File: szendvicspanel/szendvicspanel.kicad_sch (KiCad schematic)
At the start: 2 parts

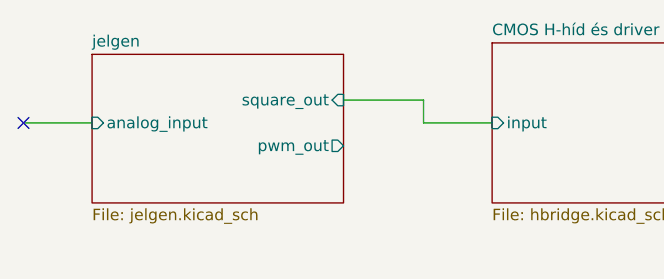
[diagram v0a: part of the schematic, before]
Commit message: Projekt átnevezése
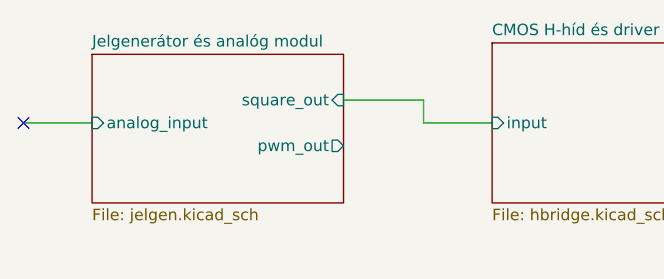
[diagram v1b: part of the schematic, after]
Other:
- sheet jelgen renamed Jelgenerátor és analóg modul
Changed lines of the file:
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@@
 			(color 0 0 0 0.0000)
 		)
-		(property "Sheetname" "jelgen"
+		(property "Sheetname" "Jelgenerátor és analóg modul"
 			(at 54.61 37.3884 0)
 			(effects
@@
 		)
 		(instances
-			(project "lebegteto_analog"
+			(project "szendvicspanel"
 				(path "/69584044-3e78-46a7-9ace-309a005e8329"
 					(page "2")
@@
 		)
 		(instances
-			(project "lebegteto_analog"
+			(project "szendvicspanel"
 				(path "/69584044-3e78-46a7-9ace-309a005e8329"
 					(page "4")

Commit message: Footprintek
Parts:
- LS1, LS2: footprint (none) -> Connector_PinHeader_1.27mm:PinHeader_1x02_P1.27mm_Horizontal
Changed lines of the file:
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@@
 			)
 		)
-		(property "Footprint" ""
+		(property "Footprint" "Connector_PinHeader_1.27mm:PinHeader_1x02_P1.27mm_Horizontal"
 			(at 181.991 55.88 0)
 			(effects
@@
 			)
 		)
-		(property "Footprint" ""
+		(property "Footprint" "Connector_PinHeader_1.27mm:PinHeader_1x02_P1.27mm_Horizontal"
 			(at 181.991 40.64 0)
 			(effects

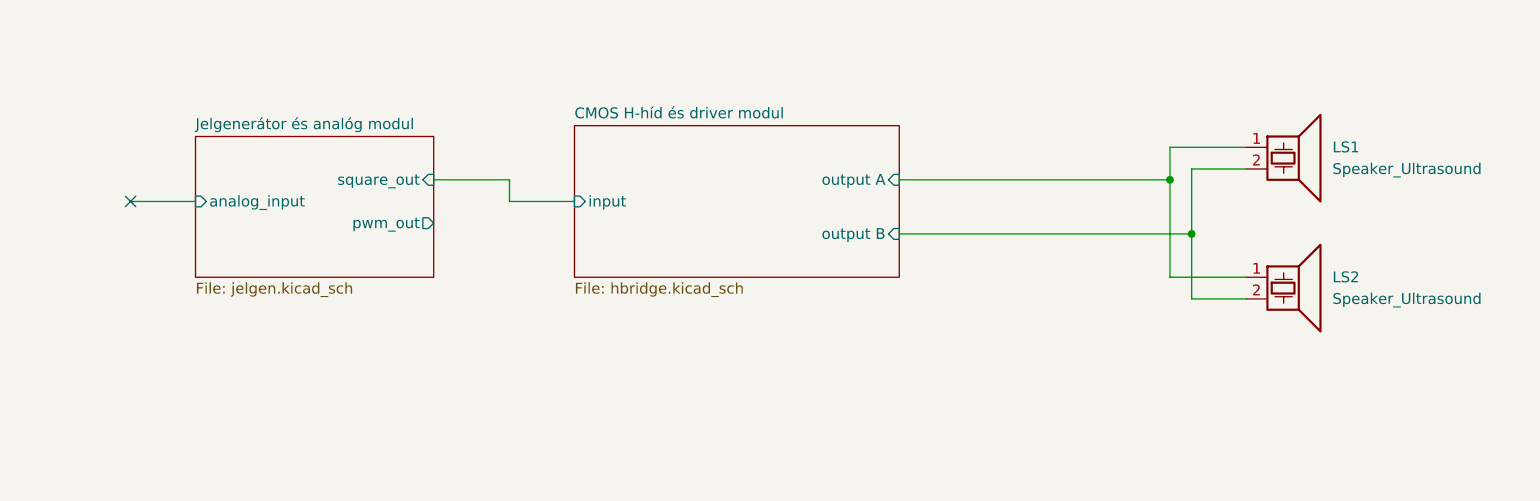
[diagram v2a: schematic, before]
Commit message: Jelgenerátor layer schematic
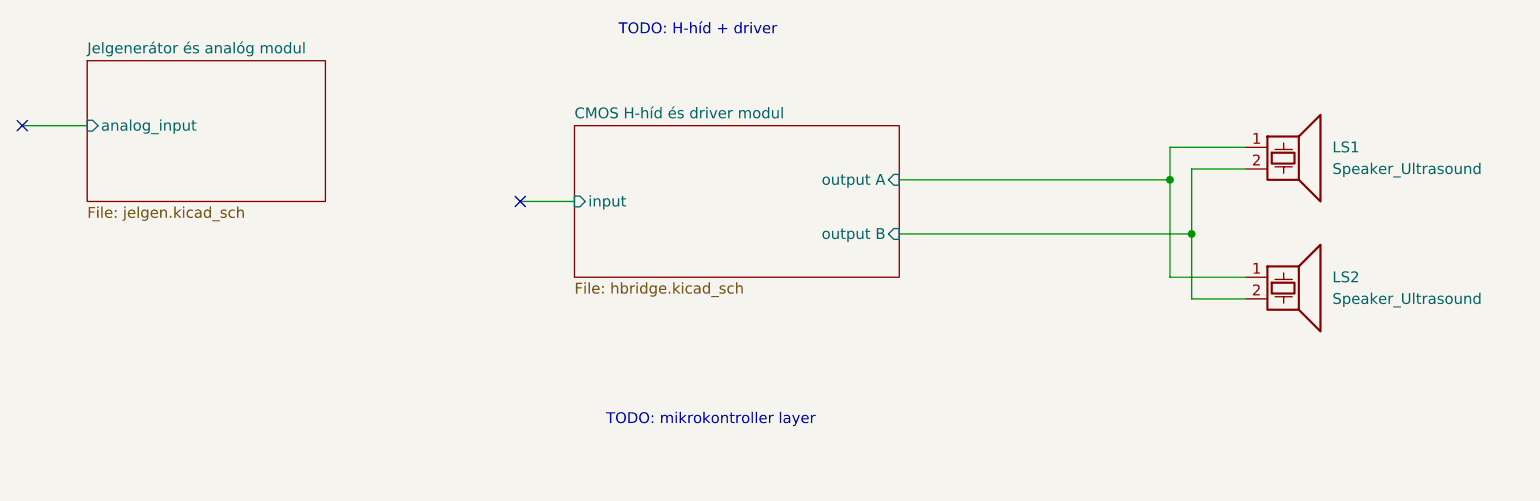
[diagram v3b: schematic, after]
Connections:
- no-connect marks 1 -> 2
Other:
- sheet Jelgenerátor és analóg modul ports: added none; removed pwm_out, square_out
- note added: "TODO: H-híd + driver"
- note added: "TODO: mikrokontroller layer"
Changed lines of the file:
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@@
 		(company "Schönherz Elektronikai Műhely")
+	)
+	(text "TODO: H-híd + driver"
+		(exclude_from_sim no)
+		(at 113.538 25.654 0)
+		(effects
+			(font
+				(size 1.27 1.27)
+			)
+		)
+	)
+	(text "TODO: mikrokontroller layer"
+		(exclude_from_sim no)
+		(at 115.062 71.374 0)
+		(effects
+			(font
+				(size 1.27 1.27)
+			)
+		)
 	)
 	(junction
@@
 	)
 	(no_connect
-		(at 46.99 45.72)
+		(at 34.29 36.83)
+	)
+	(no_connect
+		(at 92.71 45.72)
 	)
 	(wire
@@
 	(wire
 		(pts
-			(xy 91.44 43.18) (xy 91.44 45.72)
-		)
-		(stroke
-			(width 0)
-			(type default)
-		)
-	)
-	(wire
-		(pts
 			(xy 168.91 43.18) (xy 168.91 54.61)
 		)
@@
 	(wire
 		(pts
+			(xy 92.71 45.72) (xy 99.06 45.72)
+		)
+		(stroke
+			(width 0)
+			(type default)
+		)
+	)
+	(wire
+		(pts
 			(xy 177.8 57.15) (xy 171.45 57.15)
 		)
@@
 	(wire
 		(pts
-			(xy 46.99 45.72) (xy 54.61 45.72)
+			(xy 34.29 36.83) (xy 41.91 36.83)
 		)
 		(stroke
@@
 		(pts
 			(xy 168.91 39.37) (xy 177.8 39.37)
-		)
-		(stroke
-			(width 0)
-			(type default)
-		)
-	)
-	(wire
-		(pts
-			(xy 91.44 45.72) (xy 99.06 45.72)
-		)
-		(stroke
-			(width 0)
-			(type default)
-		)
-	)
-	(wire
-		(pts
-			(xy 82.55 43.18) (xy 91.44 43.18)
 		)
 		(stroke
@@
 	)
 	(sheet
-		(at 54.61 38.1)
+		(at 41.91 29.21)
 		(size 27.94 16.51)
 		(exclude_from_sim no)
@@
 		)
 		(property "Sheetname" "Jelgenerátor és analóg modul"
-			(at 54.61 37.3884 0)
+			(at 41.91 28.4984 0)
 			(effects
 				(font
@@
 		)
 		(property "Sheetfile" "jelgen.kicad_sch"
-			(at 54.61 55.1946 0)
+			(at 41.91 46.3046 0)
 			(effects
 				(font
@@
 			)
 		)
-		(pin "square_out" input
-			(at 82.55 43.18 0)
-			(effects
-				(font
-					(size 1.27 1.27)
-				)
-				(justify right)
-			)
-		)
 		(pin "analog_input" input
-			(at 54.61 45.72 180)
-			(effects
-				(font
-					(size 1.27 1.27)
-				)
-				(justify left)
-			)
-		)
-		(pin "pwm_out" output
-			(at 82.55 48.26 0)
-			(effects
-				(font
-					(size 1.27 1.27)
-				)
-				(justify right)
-			)
-		)
+			(at 41.91 36.83 180)
+			(effects
+				(font
+					(size 1.27 1.27)
+				)
+				(justify left)
+			)
+		)

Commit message: Jelgenerátor layer, README, .gitignore
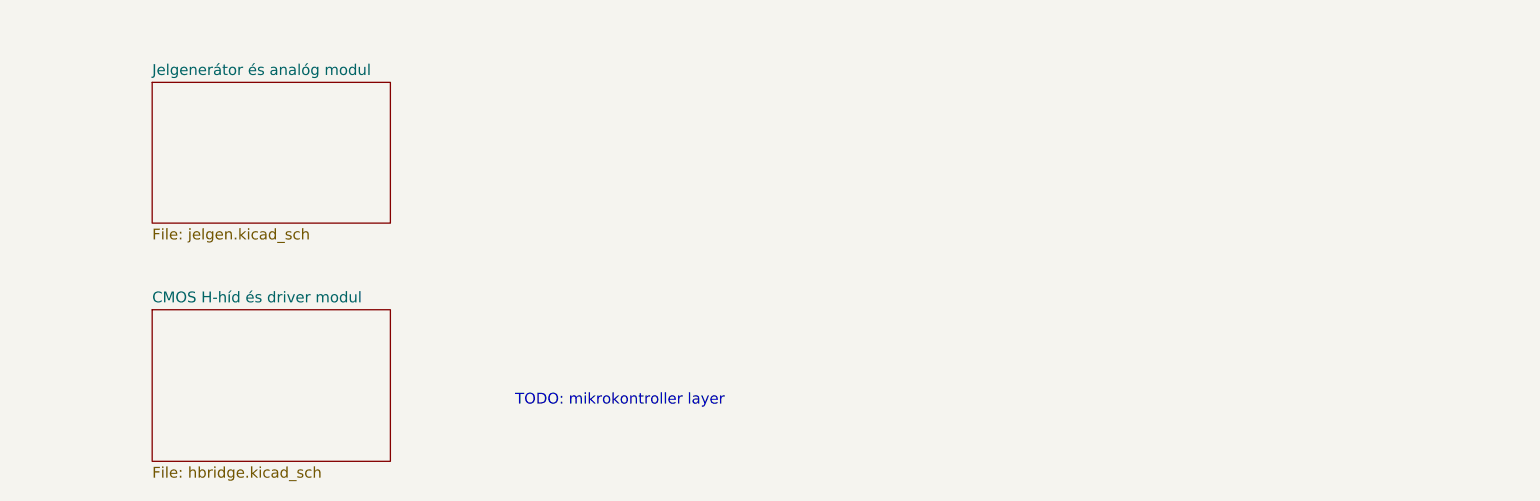
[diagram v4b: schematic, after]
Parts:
- removed LS1, LS2: Speaker_Ultrasound, Connector_PinHeader_1.27mm:PinHeader_1x02_P1.27mm_Horizontal, symbol Device:Speaker_Ultrasound
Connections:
- no-connect marks 2 -> 0
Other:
- sheet CMOS H-híd és driver modul ports: added none; removed input, output A, output B
- sheet Jelgenerátor és analóg modul ports: added none; removed analog_input
- note removed: "TODO: H-híd + driver"
